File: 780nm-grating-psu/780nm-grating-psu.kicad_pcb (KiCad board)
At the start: 4 copper layers, 101 x 58 mm, 106 parts, among them IC1 ADP7142ARDZ-5.0-R7, IC2 LT8618EDDB#TRPBF, J1 TSW-102-07-G-D, J2 1755736, J3 54-00166, J4 TSW-102-07-G-S, J7 1715747, Q1 FDD3N40TM, Q2 2N7002, Q3 2N7002, U1 LT3757AEDD, U2 ADP7142ARDZ-3.3

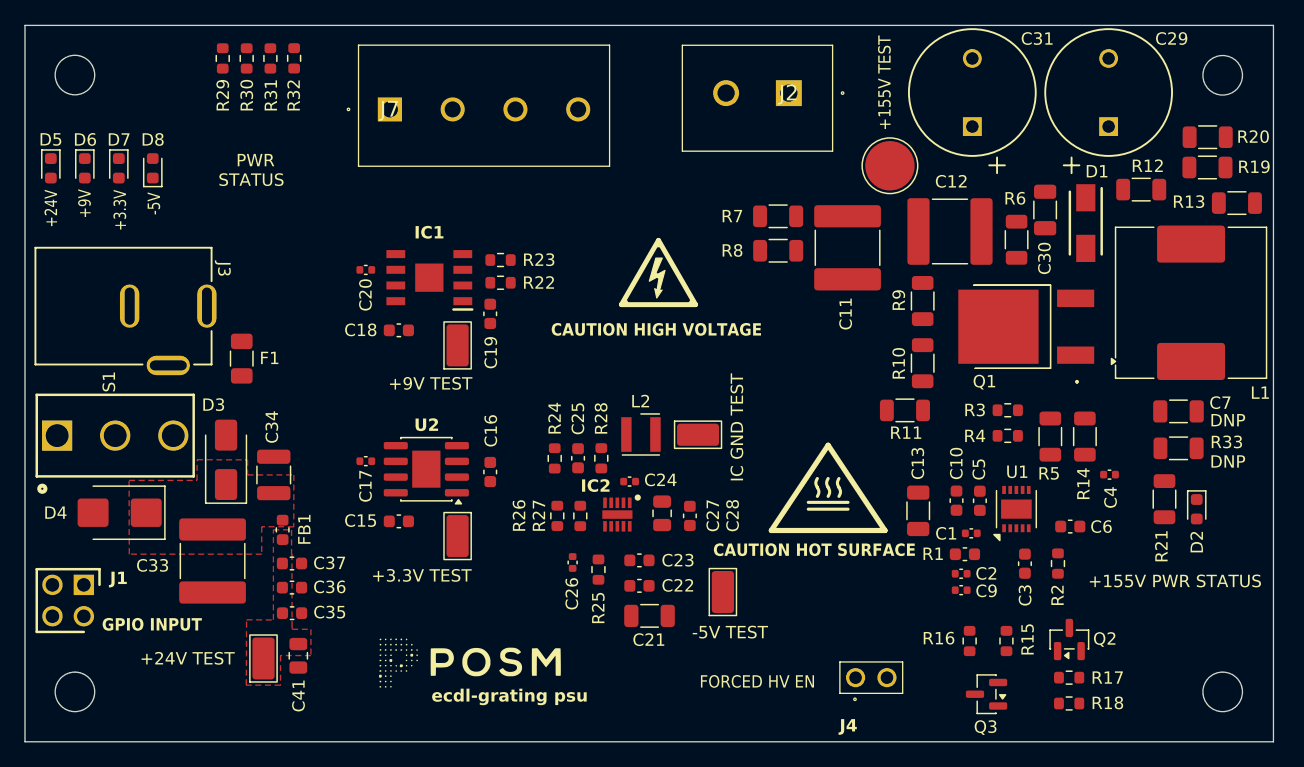
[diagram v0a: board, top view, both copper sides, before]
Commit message: layout for pcb 780nm psu pcb done! (post chip)
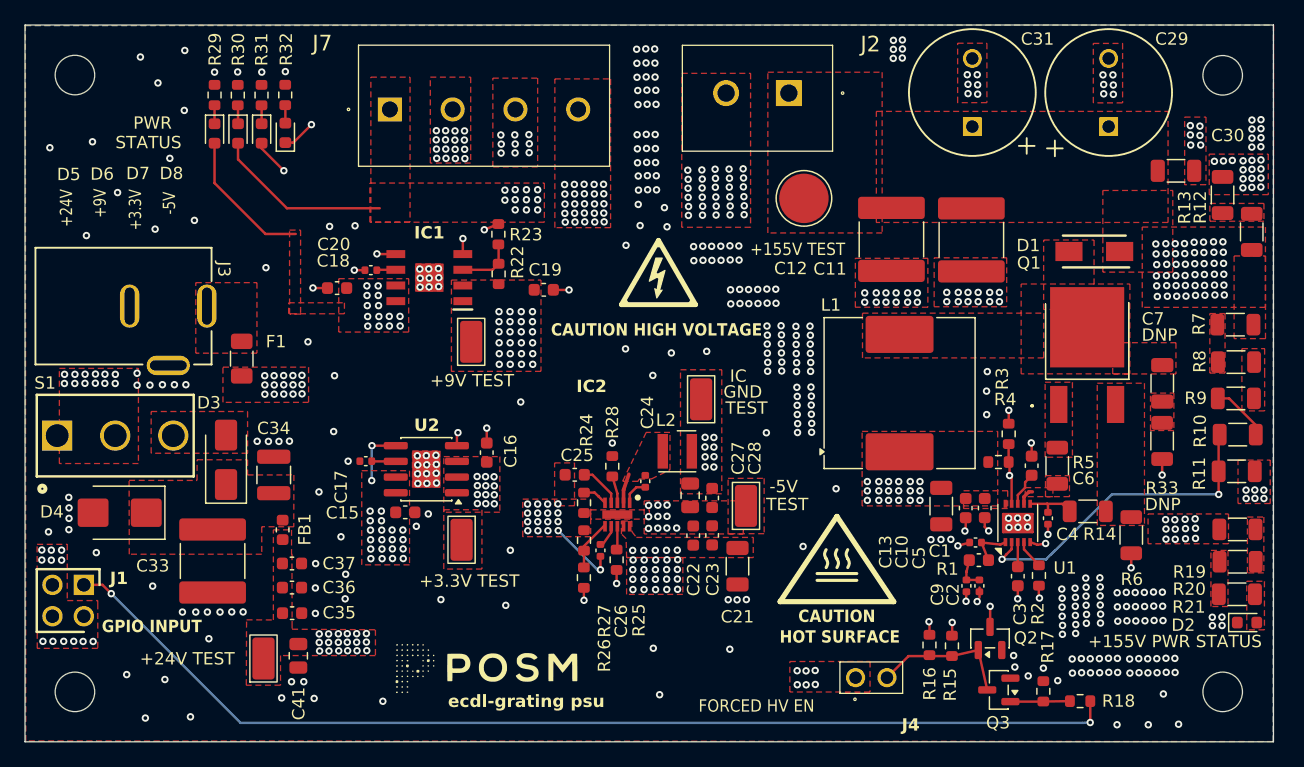
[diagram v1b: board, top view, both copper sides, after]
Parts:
- -5V: renamed from -5V TEST
- IC : renamed from IC GND TEST
- moved R8 38.1 mm to (240.3, 60.7)
- moved R7 38.0 mm to (240.3, 57.7)
- moved R20 34.4 mm to (240.4, 76.9)
- moved R19 29.4 mm to (240.4, 74.3)
- moved R11 27.3 mm to (240.4, 69.6), turned to 0 degrees
- moved R9 26.5 mm to (240.3, 63.7), turned to 180 degrees
- moved R10 26.1 mm to (240.5, 66.6), turned to 180 degrees
- moved R6 25.7 mm to (231.8, 74.8), turned to 90 degrees
- moved L1 24.7 mm to (213.1, 63.2)
- moved D5 13.5 mm to (157.7, 42.2)
- moved D6 12.7 mm to (159.6, 42.2)
- moved D7 11.9 mm to (161.5, 42.2)
- moved D8 11.1 mm to (163.4, 42.2)
- moved C30 11.1 mm to (235.5, 45.3), turned to 0 degrees
- moved C11 10.0 mm to (218.9, 50.9)
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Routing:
- net HV_EN: track 0.00 -> 87.8 mm, vias 0 -> 2
- net FBX_+155V: track 0.00 -> 25.6 mm, vias 0 -> 2
- net GND: track 0.00 -> 25.1 mm, vias 0 -> 454
- net +24V: track 0.00 -> 19.0 mm, vias 0 -> 99
- net SHDN: track 0.00 -> 17.8 mm, vias 0 -> 2
- net +9V: track 0.00 -> 14.4 mm, vias 0 -> 35
- net Net-(Q2-G): track 0.00 -> 11.5 mm
- net -5V: track 0.00 -> 8.54 mm, vias 0 -> 53
- net Net-(Q3-G): track 0.00 -> 4.82 mm
- net Net-(R10-Pad1): track 0.00 -> 4.74 mm
- net Net-(IC1-SENSE/ADJ): track 0.00 -> 4.67 mm
- net Net-(U1-SENSE): track 0.00 -> 4.17 mm
- net FB: track 0.00 -> 4.10 mm
- net Net-(IC2-INTVCC): track 0.00 -> 3.55 mm
- net Net-(U1-VC): track 0.00 -> 3.53 mm
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- added copper zone on F.Cu, net +155V
- added copper zone on In2.Cu, net +155V
- added copper zone on In2.Cu, net +24V
- added copper zone on F.Cu, net +24V_RAW1
- added copper zone on In2.Cu, net +24V_RAW1
- added copper zone on F.Cu, net +24V_RAW2
- added copper zone on F.Cu, net +3.3V
- added copper zone on In2.Cu, net +3.3V
- added copper zone on F.Cu, net +9V
- added copper zone on In2.Cu, net +9V
- added copper zone on F.Cu, net -5V
- added copper zone on In2.Cu, net -5V
- added copper zone on F.Cu, net G
- added copper zone on B.Cu, net GND
- added copper zone on F.Cu, net GND
- added copper zone on In1.Cu, net GND
- added copper zone on In2.Cu, net GND
- added copper zone on F.Cu, net Net-(C7-Pad2)
- added copper zone on F.Cu, net Net-(D1-A)
- added copper zone on F.Cu, net Net-(D2-A)
- added copper zone on F.Cu, net Net-(IC2-SW)
- added copper zone on F.Cu, net Net-(J3-A)
- added copper zone on F.Cu, net Net-(Q1-D)
- added copper zone on F.Cu, net Net-(R12-Pad2)
- added copper zone on F.Cu, net Net-(R19-Pad2)
- added copper zone on F.Cu, net Net-(R20-Pad2)
- added copper zone on F.Cu, net Net-(R7-Pad2)
- added copper zone on F.Cu, net Net-(R8-Pad2)
- added copper zone on F.Cu, net Net-(U1-GATE)
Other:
- board text added: "GND"
- board text added: "HOT SURFACE"
- board text added: "TEST"
